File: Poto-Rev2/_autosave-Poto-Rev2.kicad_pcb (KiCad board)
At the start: 2 copper layers, 323.9 x 145.3 mm, 266 parts, among them J1 TYPE-C-31-M12_13, J10 Conn_01x01, J12 Conn_01x01, J15 OLED, J2 SM04B-SRSS-TB(LF)(SN), J3 Conn_01x12, J4 RGB, J5 ENCODER, J6 USB, J7 Conn_01x12, J8 Conn_01x01, J9 Conn_01x05, Q1 S8050, SW1 RESET, U1 ATmega32U4-MU, U3 TPD4E05U06DQAR, Y1 16Mhz

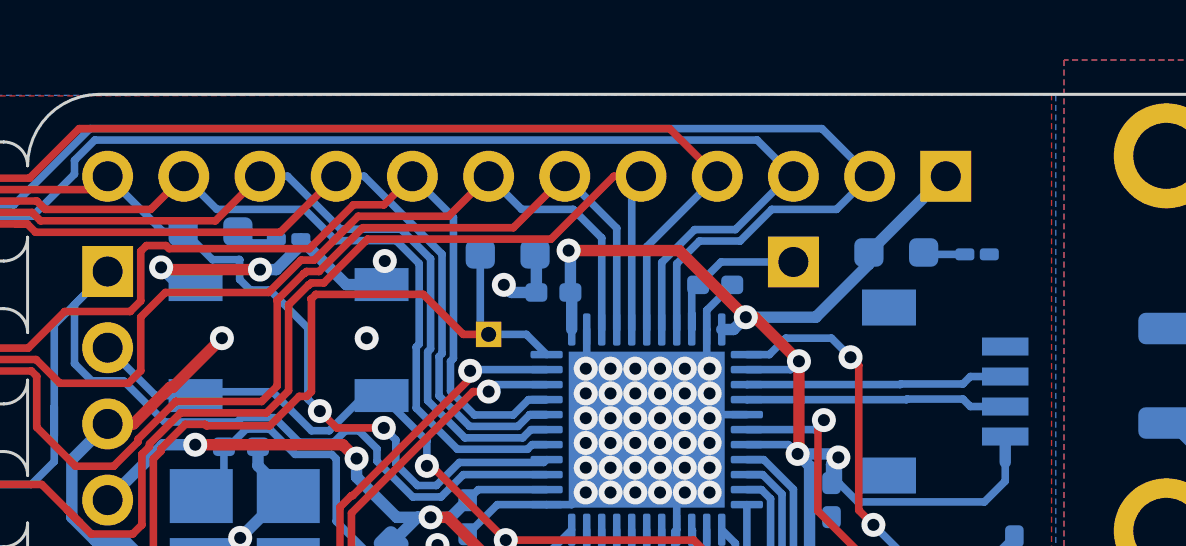
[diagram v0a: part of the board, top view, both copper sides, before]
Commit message: added some pads
added some pads for columns and rows
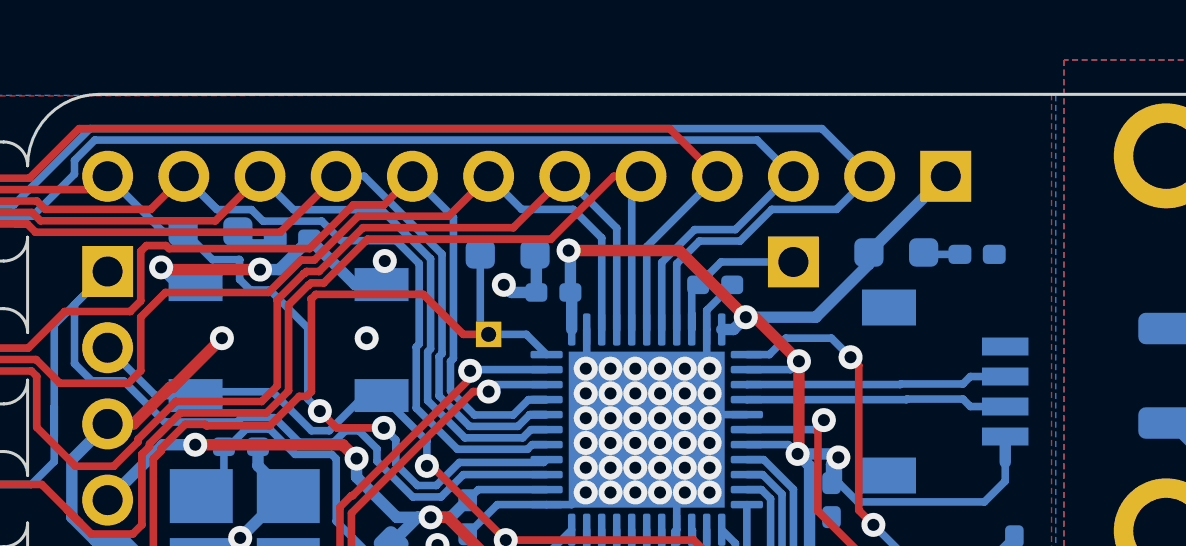
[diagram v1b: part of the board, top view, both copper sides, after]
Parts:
- LED1, LED2: footprint LED_SMD:LED_0201_0603Metric_Pad0.64x0.40mm_HandSolder -> LED_SMD:LED_0402_1005Metric_Pad0.77x0.64mm_HandSolder
- moved LED2 0.13 mm to (320.0, 90.6)
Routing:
- net DRGB: track 43.8 -> 45.3 mm
